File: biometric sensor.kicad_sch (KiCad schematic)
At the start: 5 parts, among them U1 MAX30102

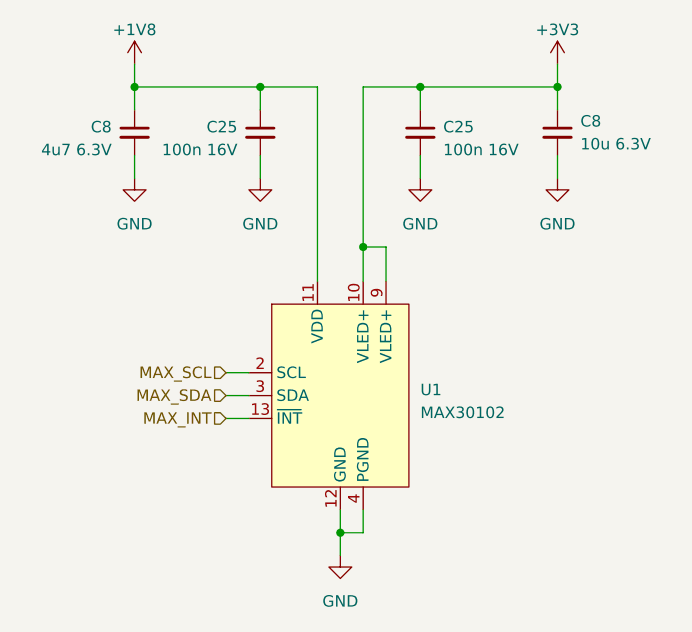
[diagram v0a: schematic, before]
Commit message: Update to KiCad 8 + Add/Fix voltage selector for nRF
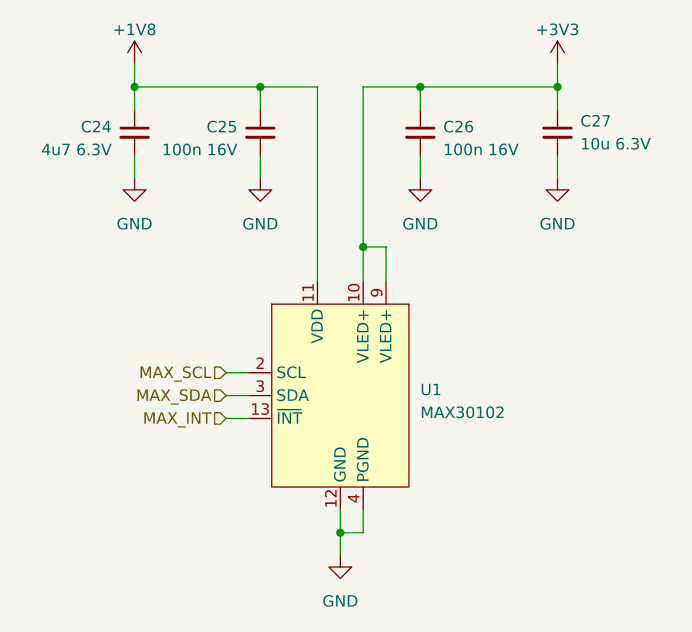
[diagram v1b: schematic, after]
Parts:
- renumbered C8 to C24, C25 to C26, C8 to C27
